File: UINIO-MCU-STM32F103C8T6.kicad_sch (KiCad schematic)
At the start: 36 parts, among them J1 Conn_01x24_Pin, J2 Conn_01x24_Pin, J3 Conn_01x04_Pin, SW1 BOOT1, SW2 NRST, SW3 BOOT0, U1 ME6211C33M5G-N, U2 STM32F103C8T6, Y1 32.768KHz, Y2 8MHz

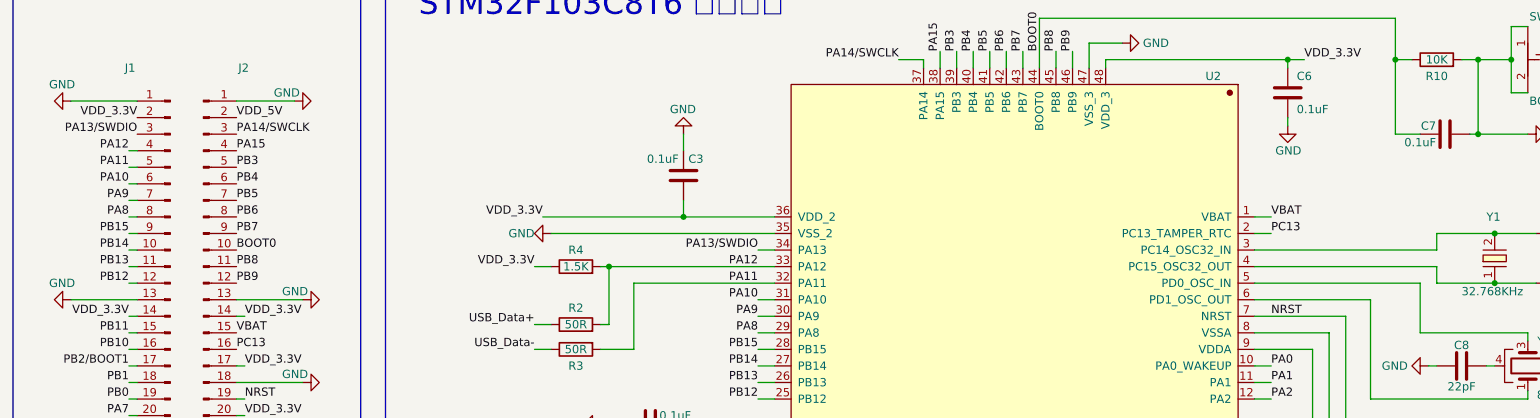
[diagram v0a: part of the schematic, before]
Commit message: Release UINIO-MCU-STM32F103C8T6 version 3.0.0.
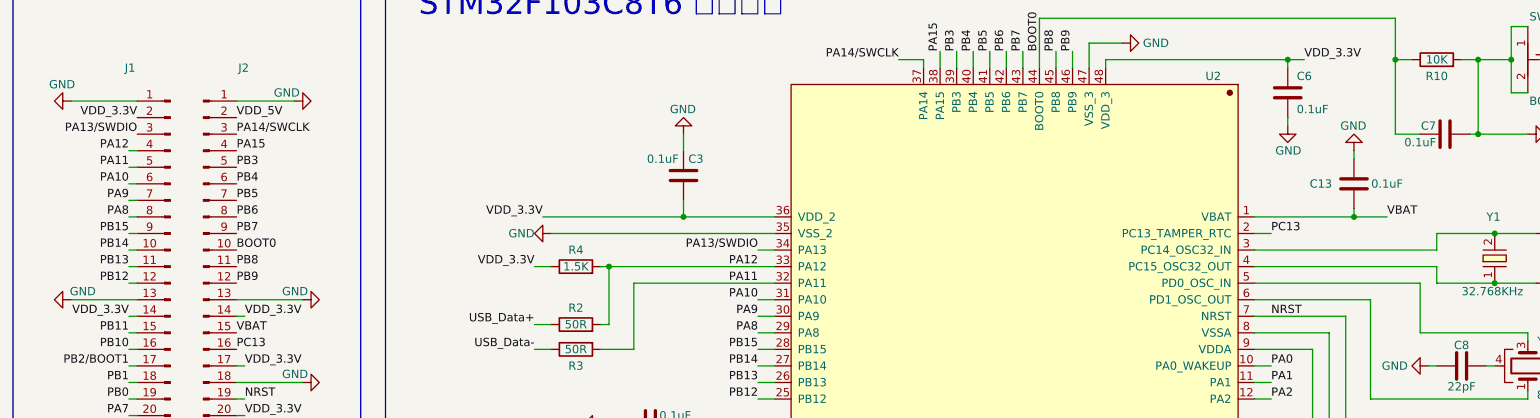
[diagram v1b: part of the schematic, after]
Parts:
- added C13: 0.1uF, Capacitor_SMD:C_0402_1005Metric, symbol Device:C
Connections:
- net GND: now also C13.1
- net VBAT: now also C13.2
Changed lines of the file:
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@@
   (title_block
     (title "UINIO-MCU-STM32F103C8T6")
-    (date "2024-02-06")
+    (date "2024-02-07")
     (rev "Version 3.0.0")
     (company "UinIO.com 电子技术工作室")
@@
   )
   (junction (at 254 93.98) (diameter 0) (color 0 0 0 0)
+  )
+  (junction (at 220.98 55.88) (diameter 0) (color 0 0 0 0)
   )
   (junction (at 210.82 31.75) (diameter 0) (color 0 0 0 0)
@@
     (stroke (width 0) (type default))
   )
-  (wire (pts (xy 208.28 55.88) (xy 205.74 55.88))
+  (wire (pts (xy 226.06 55.88) (xy 220.98 55.88))
     (stroke (width 0) (type default))
   )
@@
   )
   (wire (pts (xy 247.65 26.67) (xy 245.11 26.67))
+    (stroke (width 0) (type default))
+  )
+  (wire (pts (xy 220.98 54.61) (xy 220.98 55.88))
     (stroke (width 0) (type default))
   )
@@
     (stroke (width 0) (type default))
   )
+  (wire (pts (xy 220.98 55.88) (xy 205.74 55.88))
+    (stroke (width 0) (type default))
+  )
   (wire (pts (xy 233.68 66.04) (xy 233.68 63.5))
     (stroke (width 0) (type default))
@@
   )
   (polyline (pts (xy 118.11 16.51) (xy 280.67 16.51))
+    (stroke (width 0) (type default))
+  )
+  (wire (pts (xy 220.98 45.72) (xy 220.98 46.99))
     (stroke (width 0) (type default))
   )
@@
     (effects (font (size 1.27 1.27)) (justify right bottom))
   )
-  (label "VBAT" (at 208.28 55.88 0) (fields_autoplaced)
+  (label "VBAT" (at 226.06 55.88 0) (fields_autoplaced)
     (effects (font (size 1.27 1.27)) (justify left bottom))
   )
@@
         (path "/eeb3a4b9-cc42-48f4-a80d-47b4dcfcec11"
           (reference "C9") (unit 1)
+        )
+      )
+    )
+  )
+  (symbol (lib_id "Device:C") (at 220.98 50.8 0) (mirror y) (unit 1)
+    (in_bom yes) (on_board yes) (dnp no)
+    (property "Reference" "C13" (at 215.9 50.8 0)
+      (effects (font (size 1.27 1.27)))
+    )
+    (property "Value" "0.1uF" (at 226.06 50.8 0)
+      (effects (font (size 1.27 1.27)))
+    )
+    (property "Footprint" "Capacitor_SMD:C_0402_1005Metric" (at 220.0148 54.61 0)
+      (effects (font (size 1.27 1.27)) hide)
+    )
+    (property "Datasheet" "~" (at 220.98 50.8 0)
+      (effects (font (size 1.27 1.27)) hide)
+    )
+    (pin "1")
+    (pin "2")
+    (instances
+      (project "UINIO-MCU-STM32F103C8T6"
+        (path "/eeb3a4b9-cc42-48f4-a80d-47b4dcfcec11"
+          (reference "C13") (unit 1)
         )
       )
@@
       (effects (font (size 1.27 1.27)) hide)
     )
-    (property "Value" "GND" (at 24.765 66.04 90)
+    (property "Value" "GND" (at 27.94 67.31 90)
       (effects (font (size 1.27 1.27)) (justify right))
     )
@@
         )
       )
+    )
+  )
+  (symbol (lib_id "power:GND") (at 220.98 45.72 0) (mirror x) (unit 1)
+    (in_bom yes) (on_board yes) (dnp no)
+    (property "Reference" "#PWR030" (at 220.98 39.37 0)
+      (effects (font (size 1.27 1.27)) hide)
+    )
+    (property "Value" "GND" (at 222.885 41.91 0)
+      (effects (font (size 1.27 1.27)) (justify right))
+    )
+    (property "Footprint" "" (at 220.98 45.72 0)
+      (effects (font (size 1.27 1.27)) hide)
+    )
+    (property "Datasheet" "" (at 220.98 45.72 0)
+      (effects (font (size 1.27 1.27)) hide)
+    )
+    (pin "1")
+    (instances
+      (project "UINIO-MCU-STM32F103C8T6"
+        (path "/eeb3a4b9-cc42-48f4-a80d-47b4dcfcec11"
+          (reference "#PWR030") (unit 1)
+        )
+      )

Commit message: update
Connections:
- net GND: now also L1.1; no longer U2.8 (VSSA)
- net VDD_3.3V: now also U2.9 (VDDA); no longer L1.1
- net at L1.2: now also U2.8 (VSSA); no longer U2.9 (VDDA)
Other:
- moved on the sheet: L1
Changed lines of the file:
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@@
   (title_block
     (title "UINIO-MCU-STM32F103C8T6")
-    (date "2024-02-07")
-    (rev "Version 3.0.0")
+    (date "2024-04-12")
+    (rev "Version 3.1.0")
     (company "UinIO.com 电子技术工作室")
   )
@@
     (stroke (width 0) (type default))
   )
-  (wire (pts (xy 236.22 118.11) (xy 255.27 118.11))
+  (wire (pts (xy 214.63 118.11) (xy 257.81 118.11))
     (stroke (width 0) (type default))
   )
@@
     (stroke (width 0) (type default))
   )
+  (wire (pts (xy 238.76 113.03) (xy 248.92 113.03))
+    (stroke (width 0) (type default))
+  )
   (wire (pts (xy 80.01 149.86) (xy 49.53 149.86))
     (stroke (width 0) (type default))
@@
     (stroke (width 0) (type default))
   )
-  (wire (pts (xy 217.17 113.03) (xy 241.3 113.03))
+  (wire (pts (xy 217.17 113.03) (xy 231.14 113.03))
     (stroke (width 0) (type default))
   )
@@
   )
   (wire (pts (xy 33.02 78.74) (xy 34.29 78.74))
-    (stroke (width 0) (type default))
-  )
-  (wire (pts (xy 228.6 118.11) (xy 214.63 118.11))
     (stroke (width 0) (type default))
   )
@@
     (effects (font (size 1.27 1.27)) (justify left bottom))
   )
-  (label "VDD_3.3V" (at 255.27 118.11 0) (fields_autoplaced)
+  (label "VDD_3.3V" (at 257.81 118.11 0) (fields_autoplaced)
     (effects (font (size 1.27 1.27)) (justify left bottom))
   )
@@
     )
   )
-  (symbol (lib_id "power:GND") (at 241.3 113.03 90) (mirror x) (unit 1)
-    (in_bom yes) (on_board yes) (dnp no)
-    (property "Reference" "#PWR022" (at 247.65 113.03 0)
-      (effects (font (size 1.27 1.27)) hide)
-    )
-    (property "Value" "GND" (at 244.475 113.03 90)
+  (symbol (lib_id "power:GND") (at 248.92 113.03 90) (mirror x) (unit 1)
+    (in_bom yes) (on_board yes) (dnp no)
+    (property "Reference" "#PWR022" (at 255.27 113.03 0)
+      (effects (font (size 1.27 1.27)) hide)
+    )
+    (property "Value" "GND" (at 252.095 113.03 90)
       (effects (font (size 1.27 1.27)) (justify right))
     )
-    (property "Footprint" "" (at 241.3 113.03 0)
-      (effects (font (size 1.27 1.27)) hide)
-    )
-    (property "Datasheet" "" (at 241.3 113.03 0)
+    (property "Footprint" "" (at 248.92 113.03 0)
+      (effects (font (size 1.27 1.27)) hide)
+    )
+    (property "Datasheet" "" (at 248.92 113.03 0)
       (effects (font (size 1.27 1.27)) hide)
     )
@@
     )
   )
-  (symbol (lib_id "Device:L") (at 232.41 118.11 270) (mirror x) (unit 1)
-    (in_bom yes) (on_board yes) (dnp no)
-    (property "Reference" "L1" (at 229.87 119.38 90)
+  (symbol (lib_id "Device:L") (at 234.95 113.03 270) (mirror x) (unit 1)
+    (in_bom yes) (on_board yes) (dnp no)
+    (property "Reference" "L1" (at 240.03 111.76 90)
       (effects (font (size 1.27 1.27)) (justify right))
     )
-    (property "Value" "1KΩ 100Mhz" (at 243.84 119.38 90)
+    (property "Value" "1KΩ 100Mhz" (at 246.38 114.3 90)
       (effects (font (size 1.27 1.27)) (justify right))
     )
-    (property "Footprint" "Inductor_SMD:L_0603_1608Metric" (at 232.41 118.11 0)
-      (effects (font (size 1.27 1.27)) hide)
-    )
-    (property "Datasheet" "~" (at 232.41 118.11 0)
-      (effects (font (size 1.27 1.27)) hide)
-    )
+    (property "Footprint" "Inductor_SMD:L_0603_1608Metric" (at 234.95 113.03 0)
+      (effects (font (size 1.27 1.27)) hide)
+    )
+    (property "Datasheet" "~" (at 234.95 113.03 0)
+      (effects (font (size 1.27 1.27)) hide)
+    )

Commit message: Release UINIO-MCU-STM32F103C8T6 version 3.2.0.
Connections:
- net PA11 renamed USB_PA11-
- net PA12 renamed USB_PA12+
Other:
- moved on the sheet: C1, C10, C11, C12, C13, C3, C4, C6, C7, C8, C9, L1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

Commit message: Release UINIO-MCU-STM32F103C8T6 version 3.2.0.
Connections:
- net USB_PA11- renamed USB_PA-
- net USB_PA12+ renamed USB_PA+
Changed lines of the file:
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@@
     (effects (font (size 1.27 1.27)) (justify left bottom))
   )
-  (label "USB_PA12+" (at 116.84 63.5 0) (fields_autoplaced)
+  (label "USB_PA+" (at 116.84 63.5 0) (fields_autoplaced)
     (effects (font (size 1.27 1.27)) (justify left bottom))
   )
@@
     (effects (font (size 1.27 1.27)) (justify left bottom))
   )
-  (label "USB_PA11-" (at 116.84 66.04 0) (fields_autoplaced)
+  (label "USB_PA-" (at 116.84 66.04 0) (fields_autoplaced)
     (effects (font (size 1.27 1.27)) (justify left bottom))
   )
